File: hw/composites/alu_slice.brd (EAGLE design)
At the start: 50 x 50 mm, 13 parts, among them CON2 GENERIC-2X10

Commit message: Basic cleanups
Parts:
- moved NOT2 0.50 mm to (9.50, 0.50)
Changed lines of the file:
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@@
 <setting verticaltext="up"/>
 </settings>
-<grid distance="0.1" unitdist="mm" unit="mm" style="lines" multiple="1" display="yes" altdistance="0.02" altunitdist="mm" altunit="mm"/>
+<grid distance="0.5" unitdist="mm" unit="mm" style="lines" multiple="1" display="yes" altdistance="0.02" altunitdist="mm" altunit="mm"/>
 <layers>
 <layer number="1" name="Top" color="4" fill="1" visible="yes" active="yes"/>
@@
 <layer number="20" name="Dimension" color="15" fill="1" visible="yes" active="yes"/>
 <layer number="21" name="tPlace" color="7" fill="1" visible="yes" active="yes"/>
-<layer number="22" name="bPlace" color="7" fill="1" visible="yes" active="yes"/>
+<layer number="22" name="bPlace" color="7" fill="1" visible="no" active="yes"/>
 <layer number="23" name="tOrigins" color="15" fill="1" visible="yes" active="yes"/>
-<layer number="24" name="bOrigins" color="15" fill="1" visible="yes" active="yes"/>
+<layer number="24" name="bOrigins" color="15" fill="1" visible="no" active="yes"/>
 <layer number="25" name="tNames" color="7" fill="1" visible="no" active="yes"/>
 <layer number="26" name="bNames" color="7" fill="1" visible="no" active="yes"/>
@@
 <layer number="38" name="bTest" color="7" fill="1" visible="no" active="yes"/>
 <layer number="39" name="tKeepout" color="4" fill="11" visible="yes" active="yes"/>
-<layer number="40" name="bKeepout" color="1" fill="11" visible="yes" active="yes"/>
+<layer number="40" name="bKeepout" color="1" fill="11" visible="no" active="yes"/>
 <layer number="41" name="tRestrict" color="4" fill="10" visible="yes" active="yes"/>
-<layer number="42" name="bRestrict" color="1" fill="10" visible="yes" active="yes"/>
+<layer number="42" name="bRestrict" color="1" fill="10" visible="no" active="yes"/>
 <layer number="43" name="vRestrict" color="2" fill="10" visible="no" active="yes"/>
 <layer number="44" name="Drills" color="7" fill="1" visible="no" active="yes"/>
@@
 <layer number="49" name="Reference" color="7" fill="1" visible="no" active="yes"/>
 <layer number="50" name="dxf" color="7" fill="1" visible="no" active="no"/>
-<layer number="51" name="tDocu" color="7" fill="1" visible="no" active="yes"/>
+<layer number="51" name="tDocu" color="7" fill="1" visible="yes" active="yes"/>
 <layer number="52" name="bDocu" color="7" fill="1" visible="no" active="yes"/>
 <layer number="53" name="tGND_GNDA" color="7" fill="9" visible="no" active="no"/>
@@
 <autorouter>
 <pass name="Default">
-<param name="RoutingGrid" value="50mil"/>
-<param name="AutoGrid" value="1"/>
-<param name="Efforts" value="0"/>
-<param name="TopRouterVariant" value="1"/>
+<param name="RoutingGrid" value="0.05mm"/>
+<param name="AutoGrid" value="0"/>
+<param name="Efforts" value="2"/>
+<param name="TopRouterVariant" value="0"/>
 <param name="tpViaShape" value="round"/>
-<param name="PrefDir.1" value="|"/>
+<param name="PrefDir.1" value="-"/>
 <param name="PrefDir.2" value="0"/>
 <param name="PrefDir.3" value="0"/>
@@
 <param name="PrefDir.14" value="0"/>
 <param name="PrefDir.15" value="0"/>
-<param name="PrefDir.16" value="-"/>
+<param name="PrefDir.16" value="|"/>
 <param name="cfVia" value="8"/>
 <param name="cfNonPref" value="5"/>
@@
 <element name="SEL1" library="p.peter-gator" package="SELECTOR-2-LANE-NOMUX" value="1_BIT_SELECT" x="0.5" y="34.5"/>
 <element name="SEL3" library="p.peter-gator" package="SELECTOR-2-LANE-NOMUX" value="1_BIT_SELECT" x="12.5" y="34.5"/>
-<element name="NOT2" library="p.peter-gator" package="NOT-VERTICAL" value="NOTVERTICAL" x="9" y="0.5" rot="R90"/>
+<element name="NOT2" library="p.peter-gator" package="NOT-VERTICAL" value="NOTVERTICAL" x="9.5" y="0.5" rot="R90"/>
 <element name="NAND1" library="p.peter-gator" package="NAND" value="NAND" x="0.5" y="5"/>
 <element name="XOR4" library="p.peter-gator" package="XOR" value="XOR" x="28.5" y="19.5"/>
@@
 <wire x1="1.5" y1="32" x2="11.5" y2="34.5" width="0" layer="19" extent="1-1"/>
 <wire x1="4.5" y1="13.5" x2="1.5" y2="32" width="0" layer="19" extent="1-1"/>
-<wire x1="0.5" y1="3.5" x2="4.5" y2="13.5" width="0" layer="19" extent="1-1"/>
+<wire x1="1" y1="3.5" x2="4.5" y2="13.5" width="0" layer="19" extent="1-1"/>
 <wire x1="48" y1="5" x2="48.5" y2="32" width="0" layer="19" extent="1-1"/>
 <wire x1="39.93" y1="1.27" x2="48" y2="5" width="0" layer="19" extent="1-16"/>
@@
 <wire x1="9.5" y1="34.5" x2="13.8" y2="32" width="0" layer="19" extent="1-1"/>
 <wire x1="6.5" y1="13.5" x2="13.8" y2="32" width="0" layer="19" extent="1-1"/>
-<wire x1="0.5" y1="2.5" x2="6.5" y2="13.5" width="0" layer="19" extent="1-1"/>
+<wire x1="1" y1="2.5" x2="6.5" y2="13.5" width="0" layer="19" extent="1-1"/>
 <wire x1="46" y1="5" x2="47.5" y2="32" width="0" layer="19" extent="1-1"/>
 <wire x1="39.93" y1="1.27" x2="46" y2="5" width="0" layer="19" extent="1-1"/>
@@
 <contactref element="SEL1" pad="SEL"/>
 <contactref element="NOT2" pad="A"/>
-<wire x1="9" y1="2.5" x2="2.5" y2="34.5" width="0" layer="19" extent="1-1"/>
+<wire x1="9.5" y1="2.5" x2="2.5" y2="34.5" width="0" layer="19" extent="1-1"/>
 </signal>
 <signal name="INV_ADD">
@@
 <contactref element="NAND1" pad="A"/>
 <contactref element="NOT2" pad="NOT"/>
-<wire x1="0.5" y1="1.5" x2="3.5" y2="5" width="0" layer="19" extent="1-1"/>
+<wire x1="1" y1="1.5" x2="3.5" y2="5" width="0" layer="19" extent="1-1"/>
 </signal>
 <signal name="N$3">

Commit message: Naming cleanup
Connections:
- net CARRY renamed CARRY_OUT
- net INV_ADD renamed INVERT
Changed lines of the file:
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@@
 <wire x1="31" y1="5" x2="46.5" y2="32" width="0" layer="19" extent="1-1"/>
 </signal>
-<signal name="CARRY">
+<signal name="CARRY_OUT">
 <contactref element="XOR3" pad="XOR"/>
 <contactref element="CON2" pad="11"/>
@@
 <wire x1="9.5" y1="2.5" x2="2.5" y2="34.5" width="0" layer="19" extent="1-1"/>
 </signal>
-<signal name="INV_ADD">
+<signal name="INVERT">
 <contactref element="XOR1" pad="B"/>
 </signal>

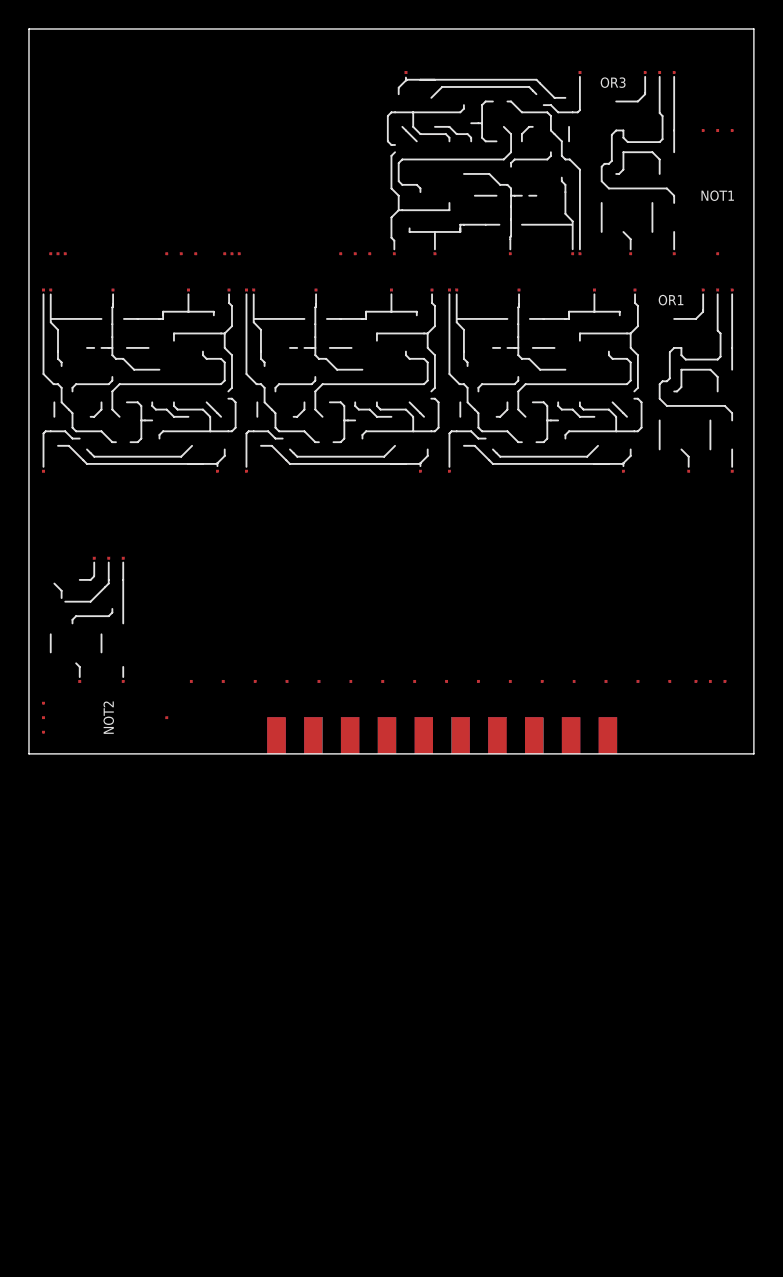
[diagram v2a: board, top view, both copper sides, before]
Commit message: Adds first orgaized integration tests
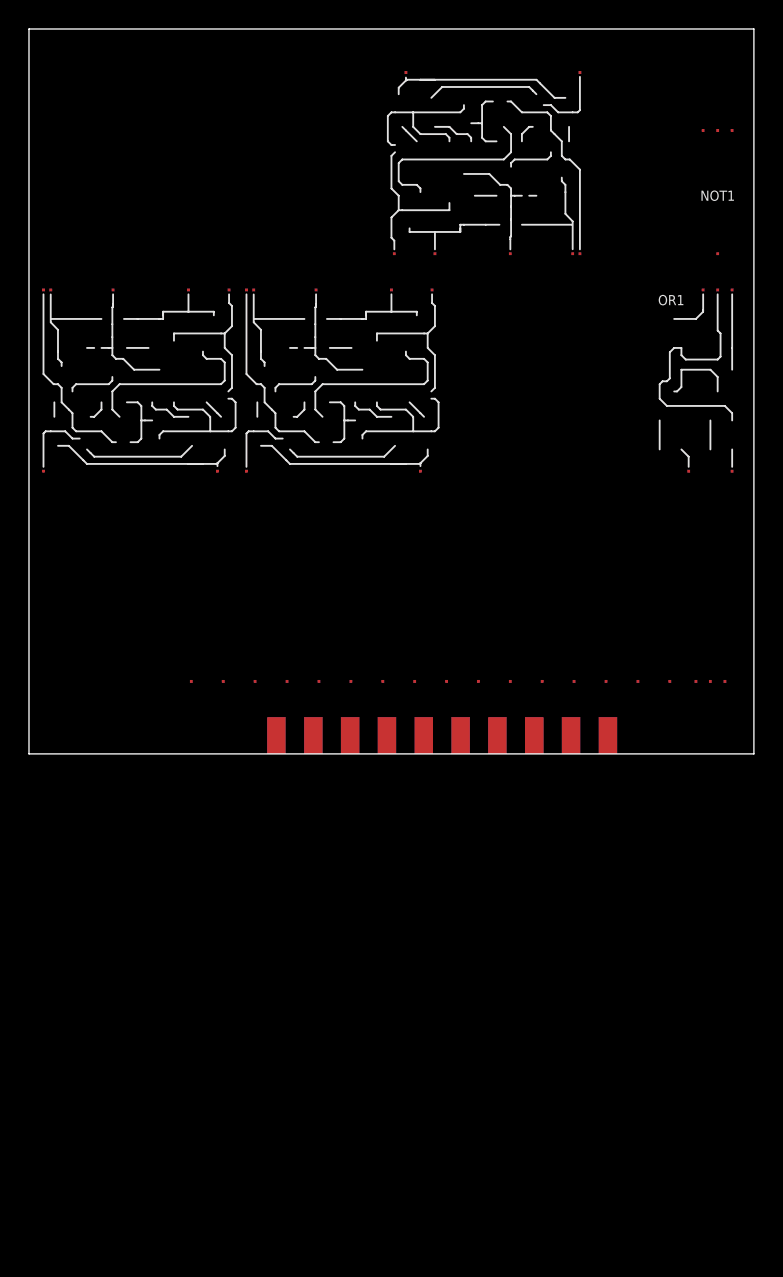
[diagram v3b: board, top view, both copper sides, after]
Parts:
- removed NAND1: NAND, p.peter-gator:NAND
- removed NOT2: NOTVERTICAL, p.peter-gator:NOT-VERTICAL
- removed OR3: OR, p.peter-gator:OR
- removed SEL1, SEL3: 1_BIT_SELECT, p.peter-gator:SELECTOR-2-LANE-NOMUX
- removed XOR4: XOR, p.peter-gator:XOR
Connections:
- net S_NOR renamed S_OR
- removed net INV_OUT: NOT2.A, SEL1.SEL
- removed net N$1: NAND1.NAND, XOR4.B
- removed net N$2: SEL1.OUT, SEL2.I1
- removed net N$3: SEL2.OUT, XOR4.A
- removed net N$7: NAND1.A, NOT2.NOT
- net +5V: no longer NAND1._VP, NOT2._VP, OR3._VP, SEL1._VP, SEL3._VP, XOR4._VP
- net A: no longer SEL3.B
- net EQUAL_IN: no longer OR3.B
- net EQUAL_OUT: no longer OR3.OR
- net GND: no longer NAND1._VN, NOT2._VN, OR3._VN, SEL1._VN, SEL3._VN, XOR4._VN
- net LEFT_IN: no longer SEL1.A, SEL3.A
- net RESULT: now also SEL2.OUT; no longer XOR4.XOR
- net RIGHT_IN: no longer SEL1.B
- net RIGHT_OUT: no longer SEL3.OUT
- net SUM: no longer OR3.A
- net S_CMP: no longer SEL3.SEL
- net S_SHIFT: no longer NAND1.B
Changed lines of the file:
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@@
 <element name="NOT1" library="p.peter-gator" package="NOT-VERTICAL" value="NOTVERTICAL" x="45.5" y="34.5"/>
 <element name="OR1" library="p.peter-gator" package="OR" value="OR" x="42.5" y="19.5"/>
-<element name="OR3" library="p.peter-gator" package="OR" value="OR" x="38.5" y="34.5"/>
 <element name="SEL2" library="p.peter-gator" package="SELECTOR-8_BIT-NOMUX" value="8_BIT_SELECT" x="10" y="5"/>
-<element name="SEL1" library="p.peter-gator" package="SELECTOR-2-LANE-NOMUX" value="1_BIT_SELECT" x="0.5" y="34.5"/>
-<element name="SEL3" library="p.peter-gator" package="SELECTOR-2-LANE-NOMUX" value="1_BIT_SELECT" x="12.5" y="34.5"/>
-<element name="NOT2" library="p.peter-gator" package="NOT-VERTICAL" value="NOTVERTICAL" x="9.5" y="0.5" rot="R90"/>
-<element name="NAND1" library="p.peter-gator" package="NAND" value="NAND" x="0.5" y="5"/>
-<element name="XOR4" library="p.peter-gator" package="XOR" value="XOR" x="28.5" y="19.5"/>
 <element name="CON2" library="p.peter-connectors" package="PINHEADER-100MIL-2X10-EDGE" value="GENERIC-2X10" x="28.5" y="0"/>
 </elements>
@@
 <contactref element="XOR2" pad="A"/>
 <contactref element="SEL2" pad="I4"/>
-<contactref element="SEL3" pad="B"/>
 <contactref element="CON2" pad="10"/>
-<wire x1="14" y1="34.5" x2="26" y2="47" width="0" layer="19" extent="1-1"/>
-<wire x1="26.6" y1="5" x2="14" y2="34.5" width="0" layer="19" extent="1-1"/>
+<wire x1="26.6" y1="5" x2="26" y2="47" width="0" layer="19" extent="1-1"/>
 <wire x1="27.23" y1="1.27" x2="26.6" y2="5" width="0" layer="19" extent="1-1"/>
 </signal>
@@
 <signal name="SUM">
 <contactref element="OR1" pad="OR"/>
-<contactref element="OR3" pad="A"/>
 <contactref element="SEL2" pad="I5"/>
-<wire x1="41.5" y1="34.5" x2="46.5" y2="32" width="0" layer="19" extent="1-1"/>
 <wire x1="31" y1="5" x2="46.5" y2="32" width="0" layer="19" extent="1-1"/>
 </signal>
@@
 <contactref element="XOR3" pad="_VP"/>
 <contactref element="OR1" pad="_VP"/>
-<contactref element="OR3" pad="_VP"/>
 <contactref element="SEL2" pad="_VP"/>
-<contactref element="SEL1" pad="_VP"/>
-<contactref element="SEL3" pad="_VP"/>
-<contactref element="NOT2" pad="_VP"/>
-<contactref element="NAND1" pad="_VP"/>
-<contactref element="XOR4" pad="_VP"/>
 <contactref element="CON2" pad="19"/>
-<wire x1="44.5" y1="47" x2="48.5" y2="43" width="0" layer="19" extent="1-1"/>
 <wire x1="48.5" y1="32" x2="48.5" y2="43" width="0" layer="19" extent="1-1"/>
 <wire x1="37.5" y1="34.5" x2="48.5" y2="32" width="0" layer="19" extent="1-1"/>
-<wire x1="29.5" y1="32" x2="37.5" y2="34.5" width="0" layer="19" extent="1-1"/>
-<wire x1="23.5" y1="34.5" x2="29.5" y2="32" width="0" layer="19" extent="1-1"/>
-<wire x1="15.5" y1="32" x2="23.5" y2="34.5" width="0" layer="19" extent="1-1"/>
-<wire x1="11.5" y1="34.5" x2="15.5" y2="32" width="0" layer="19" extent="1-1"/>
-<wire x1="1.5" y1="32" x2="11.5" y2="34.5" width="0" layer="19" extent="1-1"/>
-<wire x1="4.5" y1="13.5" x2="1.5" y2="32" width="0" layer="19" extent="1-1"/>
-<wire x1="1" y1="3.5" x2="4.5" y2="13.5" width="0" layer="19" extent="1-1"/>
+<wire x1="15.5" y1="32" x2="37.5" y2="34.5" width="0" layer="19" extent="1-1"/>
+<wire x1="1.5" y1="32" x2="15.5" y2="32" width="0" layer="19" extent="1-1"/>
 <wire x1="48" y1="5" x2="48.5" y2="32" width="0" layer="19" extent="1-1"/>
 <wire x1="39.93" y1="1.27" x2="48" y2="5" width="0" layer="19" extent="1-16"/>
@@
 <contactref element="XOR3" pad="_VN"/>
 <contactref element="OR1" pad="_VN"/>
-<contactref element="OR3" pad="_VN"/>
-<contactref element="SEL1" pad="_VN"/>
 <contactref element="SEL2" pad="_VN"/>
-<contactref element="SEL3" pad="_VN"/>
-<contactref element="NOT2" pad="_VN"/>
-<contactref element="NAND1" pad="_VN"/>
-<contactref element="XOR4" pad="_VN"/>
 <contactref element="CON2" pad="20"/>
-<wire x1="47.5" y1="43" x2="43.5" y2="47" width="0" layer="19" extent="1-1"/>
 <wire x1="47.5" y1="32" x2="47.5" y2="43" width="0" layer="19" extent="1-1"/>
-<wire x1="41.8" y1="32" x2="47.5" y2="32" width="0" layer="19" extent="1-1"/>
-<wire x1="27.8" y1="32" x2="41.8" y2="32" width="0" layer="19" extent="1-1"/>
+<wire x1="27.8" y1="32" x2="47.5" y2="32" width="0" layer="19" extent="1-1"/>
 <wire x1="25.2" y1="34.5" x2="27.8" y2="32" width="0" layer="19" extent="1-1"/>
-<wire x1="21.5" y1="34.5" x2="25.2" y2="34.5" width="0" layer="19" extent="1-1"/>
-<wire x1="13.8" y1="32" x2="21.5" y2="34.5" width="0" layer="19" extent="1-1"/>
-<wire x1="9.5" y1="34.5" x2="13.8" y2="32" width="0" layer="19" extent="1-1"/>
-<wire x1="6.5" y1="13.5" x2="13.8" y2="32" width="0" layer="19" extent="1-1"/>
-<wire x1="1" y1="2.5" x2="6.5" y2="13.5" width="0" layer="19" extent="1-1"/>
+<wire x1="13.8" y1="32" x2="25.2" y2="34.5" width="0" layer="19" extent="1-1"/>
 <wire x1="46" y1="5" x2="47.5" y2="32" width="0" layer="19" extent="1-1"/>
 <wire x1="39.93" y1="1.27" x2="46" y2="5" width="0" layer="19" extent="1-1"/>
@@
 <wire x1="19.61" y1="1.27" x2="17.8" y2="5" width="0" layer="19" extent="1-16"/>
 </signal>
-<signal name="INV_OUT">
-<contactref element="SEL1" pad="SEL"/>
-<contactref element="NOT2" pad="A"/>
-<wire x1="9.5" y1="2.5" x2="2.5" y2="34.5" width="0" layer="19" extent="1-1"/>
-</signal>
 <signal name="INVERT">
 <contactref element="XOR1" pad="B"/>
@@
 <signal name="LEFT_IN">
 <contactref element="SEL2" pad="I3"/>
-<contactref element="SEL1" pad="A"/>
-<contactref element="SEL3" pad="A"/>
 <contactref element="CON2" pad="7"/>
-<wire x1="1.5" y1="34.5" x2="13.5" y2="34.5" width="0" layer="19" extent="1-1"/>
-<wire x1="22.2" y1="5" x2="13.5" y2="34.5" width="0" layer="19" extent="1-1"/>
 <wire x1="24.69" y1="1.27" x2="22.2" y2="5" width="0" layer="19" extent="1-16"/>
 </signal>
 <signal name="EQUAL_IN">
-<contactref element="OR3" pad="B"/>
 <contactref element="CON2" pad="13"/>
-<wire x1="32.31" y1="1.27" x2="44.5" y2="34.5" width="0" layer="19" extent="1-16"/>
 </signal>
 <signal name="EQUAL_OUT">
-<contactref element="OR3" pad="OR"/>
 <contactref element="CON2" pad="17"/>
-<wire x1="37.39" y1="1.27" x2="42.5" y2="47" width="0" layer="19" extent="1-16"/>
 </signal>
 <signal name="RIGHT_IN">
-<contactref element="SEL1" pad="B"/>
 <contactref element="CON2" pad="1"/>
-<wire x1="17.07" y1="1.27" x2="2" y2="34.5" width="0" layer="19" extent="1-16"/>
 </signal>
 <signal name="RIGHT_OUT">
-<contactref element="SEL3" pad="OUT"/>
 <contactref element="CON2" pad="9"/>
-<wire x1="27.23" y1="1.27" x2="22.5" y2="34.5" width="0" layer="19" extent="1-16"/>
 </signal>
 <signal name="N$6">
@@
 <wire x1="15" y1="32" x2="45.5" y2="19.5" width="0" layer="19" extent="1-1"/>
 </signal>
-<signal name="S_NOR">
+<signal name="S_OR">
 <contactref element="SEL2" pad="S7"/>
 <contactref element="CON2" pad="16"/>
@@
 <signal name="S_CMP">
 <contactref element="SEL2" pad="S3"/>
-<contactref element="SEL3" pad="SEL"/>
 <contactref element="CON2" pad="6"/>
-<wire x1="20" y1="5" x2="14.5" y2="34.5" width="0" layer="19" extent="1-1"/>
 <wire x1="22.15" y1="1.27" x2="20" y2="5" width="0" layer="19" extent="1-1"/>
 </signal>
@@
 <signal name="S_SHIFT">
 <contactref element="SEL2" pad="S1"/>
-<contactref element="NAND1" pad="B"/>
 <contactref element="CON2" pad="2"/>
 <wire x1="11.2" y1="5" x2="17.07" y2="1.27" width="0" layer="19" extent="1-1"/>
-<wire x1="6.5" y1="5" x2="11.2" y2="5" width="0" layer="19" extent="1-1"/>
-</signal>
-<signal name="N$2">
-<contactref element="SEL1" pad="OUT"/>
-<contactref element="SEL2" pad="I1"/>
-<wire x1="13.4" y1="5" x2="10.5" y2="34.5" width="0" layer="19" extent="1-1"/>
-</signal>
-<signal name="N$1">
-<contactref element="XOR4" pad="B"/>
-<contactref element="NAND1" pad="NAND"/>
-<wire x1="5.5" y1="13.5" x2="29" y2="19.5" width="0" layer="19" extent="1-1"/>
-</signal>
-<signal name="N$7">
-<contactref element="NAND1" pad="A"/>
-<contactref element="NOT2" pad="NOT"/>
-<wire x1="1" y1="1.5" x2="3.5" y2="5" width="0" layer="19" extent="1-1"/>
-</signal>
-<signal name="N$3">
-<contactref element="SEL2" pad="OUT"/>
-<contactref element="XOR4" pad="A"/>
-<wire x1="47" y1="5" x2="41" y2="19.5" width="0" layer="19" extent="1-1"/>
 </signal>
 <signal name="OVERFLOW">
@@
 </signal>
 <signal name="RESULT">
-<contactref element="XOR4" pad="XOR"/>
 <contactref element="CON2" pad="15"/>
-<wire x1="34.85" y1="1.27" x2="39" y2="32" width="0" layer="19" extent="1-16"/>
+<contactref element="SEL2" pad="OUT"/>
+<wire x1="34.85" y1="1.27" x2="47" y2="5" width="0" layer="19" extent="1-16"/>
 </signal>
 <signal name="N$4">

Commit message: fixes some offset and juction issues
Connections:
- net LEFT_IN: now also SEL2.I1
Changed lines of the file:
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@@
 <contactref element="SEL2" pad="I3"/>
 <contactref element="CON2" pad="7"/>
+<contactref element="SEL2" pad="I1"/>
 <wire x1="24.69" y1="1.27" x2="22.2" y2="5" width="0" layer="19" extent="1-16"/>
+<wire x1="13.4" y1="5" x2="22.2" y2="5" width="0" layer="19" extent="1-1"/>
 </signal>
 <signal name="EQUAL_IN">

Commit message: Added tests for addition
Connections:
- net CARRY_OUT: now also OR1.OR; no longer XOR3.XOR
- net SUM: now also XOR3.XOR; no longer OR1.OR
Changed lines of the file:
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@@
 </signal>
 <signal name="SUM">
-<contactref element="OR1" pad="OR"/>
 <contactref element="SEL2" pad="I5"/>
-<wire x1="31" y1="5" x2="46.5" y2="32" width="0" layer="19" extent="1-1"/>
+<contactref element="XOR3" pad="XOR"/>
+<wire x1="31" y1="5" x2="25" y2="32" width="0" layer="19" extent="1-1"/>
 </signal>
 <signal name="CARRY_OUT">
-<contactref element="XOR3" pad="XOR"/>
 <contactref element="CON2" pad="11"/>
-<wire x1="29.77" y1="1.27" x2="25" y2="32" width="0" layer="19" extent="1-16"/>
+<contactref element="OR1" pad="OR"/>
+<wire x1="29.77" y1="1.27" x2="46.5" y2="32" width="0" layer="19" extent="1-16"/>
 </signal>
 <signal name="+5V">
